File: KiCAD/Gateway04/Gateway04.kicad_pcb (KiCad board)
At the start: 2 copper layers, 53 x 53 mm, 8 parts, among them U1 LSHM, U2 LSHM, U3 LSHM, U4 LSHM, U5 LSHM, U6 LSHM, U7 LSHM, U8 LSHM

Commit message: finished Gateway04
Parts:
- U1, U2, U3, U4, U5, U6, U7, U8: footprint Gateway03:LSHM-120-02.5-L-DV-A-S-TR -> Gateway04:LSHM-120-02.5-L-DV-A-S-TR
- moved U1 0.50 mm to (85.2, 83.8)
- moved U3 0.50 mm to (102.5, 83.8)
- moved U6 0.50 mm to (85.2, 110.7)
- moved U8 0.50 mm to (102.5, 110.7)
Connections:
- U1 pad 40: Net-(U1-Pad40) -> GND
- U2 pad 10: Net-(U1-Pad10) -> Net-(U1-Pad8)
- U2 pad 12: Net-(U1-Pad12) -> Net-(U1-Pad10)
- U2 pad 14: Net-(U1-Pad14) -> Net-(U1-Pad12)
- U2 pad 16: Net-(U1-Pad16) -> Net-(U1-Pad14)
- U2 pad 18: Net-(U1-Pad18) -> Net-(U1-Pad16)
- U2 pad 2: Net-(U1-Pad2) -> GND
- U2 pad 20: Net-(U1-Pad20) -> Net-(U1-Pad18)
- U2 pad 22: Net-(U1-Pad22) -> Net-(U1-Pad20)
- U2 pad 24: Net-(U1-Pad24) -> Net-(U1-Pad22)
- U2 pad 26: Net-(U1-Pad26) -> Net-(U1-Pad24)
- U2 pad 28: Net-(U1-Pad28) -> Net-(U1-Pad26)
- U2 pad 30: Net-(U1-Pad30) -> Net-(U1-Pad28)
- U2 pad 32: Net-(U1-Pad32) -> Net-(U1-Pad30)
- U2 pad 34: Net-(U1-Pad34) -> Net-(U1-Pad32)
- U2 pad 36: Net-(U1-Pad36) -> Net-(U1-Pad34)
- U2 pad 38: Net-(U1-Pad38) -> Net-(U1-Pad36)
- U2 pad 4: Net-(U1-Pad4) -> Net-(U1-Pad2)
- U2 pad 40: Net-(U1-Pad40) -> Net-(U1-Pad38)
- U2 pad 6: Net-(U1-Pad6) -> Net-(U1-Pad4)
- U2 pad 8: Net-(U1-Pad8) -> Net-(U1-Pad6)
- U3 pad 40: Net-(U3-Pad40) -> GND
- U4 pad 10: Net-(U3-Pad10) -> Net-(U3-Pad8)
- U4 pad 12: Net-(U3-Pad12) -> Net-(U3-Pad10)
- U4 pad 14: Net-(U3-Pad14) -> Net-(U3-Pad12)
- U4 pad 16: Net-(U3-Pad16) -> Net-(U3-Pad14)
- U4 pad 18: Net-(U3-Pad18) -> Net-(U3-Pad16)
- U4 pad 2: Net-(U3-Pad2) -> GND
- U4 pad 20: Net-(U3-Pad20) -> Net-(U3-Pad18)
- U4 pad 22: Net-(U3-Pad22) -> Net-(U3-Pad20)
- U4 pad 24: Net-(U3-Pad24) -> Net-(U3-Pad22)
- U4 pad 26: Net-(U3-Pad26) -> Net-(U3-Pad24)
- U4 pad 28: Net-(U3-Pad28) -> Net-(U3-Pad26)
- U4 pad 30: Net-(U3-Pad30) -> Net-(U3-Pad28)
- U4 pad 32: Net-(U3-Pad32) -> Net-(U3-Pad30)
- U4 pad 34: Net-(U3-Pad34) -> Net-(U3-Pad32)
- U4 pad 36: Net-(U3-Pad36) -> Net-(U3-Pad34)
- U4 pad 38: Net-(U3-Pad38) -> Net-(U3-Pad36)
- U4 pad 4: Net-(U3-Pad4) -> Net-(U3-Pad2)
- U4 pad 40: Net-(U3-Pad40) -> Net-(U3-Pad38)
- U4 pad 6: Net-(U3-Pad6) -> Net-(U3-Pad4)
- U4 pad 8: Net-(U3-Pad8) -> Net-(U3-Pad6)
- U5 pad 40: Net-(U5-Pad40) -> GND
- U6 pad 10: Net-(U5-Pad10) -> Net-(U5-Pad8)
- U6 pad 12: Net-(U5-Pad12) -> Net-(U5-Pad10)
- U6 pad 14: Net-(U5-Pad14) -> Net-(U5-Pad12)
- U6 pad 16: Net-(U5-Pad16) -> Net-(U5-Pad14)
- U6 pad 18: Net-(U5-Pad18) -> Net-(U5-Pad16)
- U6 pad 2: Net-(U5-Pad2) -> GND
- U6 pad 20: Net-(U5-Pad20) -> Net-(U5-Pad18)
- U6 pad 22: Net-(U5-Pad22) -> Net-(U5-Pad20)
- U6 pad 24: Net-(U5-Pad24) -> Net-(U5-Pad22)
- U6 pad 26: Net-(U5-Pad26) -> Net-(U5-Pad24)
- U6 pad 28: Net-(U5-Pad28) -> Net-(U5-Pad26)
- U6 pad 30: Net-(U5-Pad30) -> Net-(U5-Pad28)
- U6 pad 32: Net-(U5-Pad32) -> Net-(U5-Pad30)
- U6 pad 34: Net-(U5-Pad34) -> Net-(U5-Pad32)
- U6 pad 36: Net-(U5-Pad36) -> Net-(U5-Pad34)
- U6 pad 38: Net-(U5-Pad38) -> Net-(U5-Pad36)
- U6 pad 4: Net-(U5-Pad4) -> Net-(U5-Pad2)
- U6 pad 40: Net-(U5-Pad40) -> Net-(U5-Pad38)
- U6 pad 6: Net-(U5-Pad6) -> Net-(U5-Pad4)
- U6 pad 8: Net-(U5-Pad8) -> Net-(U5-Pad6)
- U7 pad 40: Net-(U7-Pad40) -> GND
- U8 pad 10: Net-(U7-Pad10) -> Net-(U7-Pad8)
- U8 pad 12: Net-(U7-Pad12) -> Net-(U7-Pad10)
- U8 pad 14: Net-(U7-Pad14) -> Net-(U7-Pad12)
- U8 pad 16: Net-(U7-Pad16) -> Net-(U7-Pad14)
- U8 pad 18: Net-(U7-Pad18) -> Net-(U7-Pad16)
- U8 pad 2: Net-(U7-Pad2) -> GND
- U8 pad 20: Net-(U7-Pad20) -> Net-(U7-Pad18)
- U8 pad 22: Net-(U7-Pad22) -> Net-(U7-Pad20)
- U8 pad 24: Net-(U7-Pad24) -> Net-(U7-Pad22)
- U8 pad 26: Net-(U7-Pad26) -> Net-(U7-Pad24)
- U8 pad 28: Net-(U7-Pad28) -> Net-(U7-Pad26)
- U8 pad 30: Net-(U7-Pad30) -> Net-(U7-Pad28)
- U8 pad 32: Net-(U7-Pad32) -> Net-(U7-Pad30)
- U8 pad 34: Net-(U7-Pad34) -> Net-(U7-Pad32)
- U8 pad 36: Net-(U7-Pad36) -> Net-(U7-Pad34)
- U8 pad 38: Net-(U7-Pad38) -> Net-(U7-Pad36)
- U8 pad 4: Net-(U7-Pad4) -> Net-(U7-Pad2)
- U8 pad 40: Net-(U7-Pad40) -> Net-(U7-Pad38)
- U8 pad 6: Net-(U7-Pad6) -> Net-(U7-Pad4)
- U8 pad 8: Net-(U7-Pad8) -> Net-(U7-Pad6)
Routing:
- net Net-(U5-Pad40): track 8.09 -> 0.00 mm, vias 1 -> 0
- net Net-(U3-Pad2): track 0.00 -> 7.28 mm, vias 0 -> 1
- net Net-(U3-Pad38): track 0.16 -> 7.34 mm
- net Net-(U7-Pad40): track 7.09 -> 0.00 mm, vias 1 -> 0
- net Net-(U1-Pad40): track 7.09 -> 0.00 mm, vias 1 -> 0
- net Net-(U3-Pad6): track 0.00 -> 6.76 mm
- net Net-(U3-Pad34): track 0.00 -> 6.75 mm
- net Net-(U3-Pad4): track 0.16 -> 6.90 mm
- net Net-(U3-Pad8): track 0.00 -> 6.63 mm
- net Net-(U3-Pad36): track 0.29 -> 6.90 mm
- net Net-(U3-Pad32): track 0.00 -> 6.61 mm
- net Net-(U3-Pad10): track 0.00 -> 6.49 mm
- net Net-(U3-Pad30): track 0.00 -> 6.47 mm
- net Net-(U3-Pad12): track 0.00 -> 6.35 mm
- net Net-(U3-Pad28): track 0.00 -> 6.34 mm
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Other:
- board text added: "Feb 2020"
- board text added: "Gateway04"
- board text removed: "Gateway03"
- board text removed: "Nov 2019"

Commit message: created gateway04
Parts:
- U1, U2, U3, U4, U5, U6, U7, U8: value LSHM -> LSHM-120-02.5-L-DV-A-S-TR; footprint Gateway04:LSHM-120-02.5-L-DV-A-S-TR -> Gateway03:LSHM-120-02.5-L-DV-A-S-TR
- moved U1 2.12 mm to (83.7, 85.3)
- moved U3 2.12 mm to (104.0, 85.3)
- moved U6 2.12 mm to (83.7, 109.2)
- moved U8 2.12 mm to (104.0, 109.2)
- moved U2 1.80 mm to (83.7, 94.8)
- moved U4 1.80 mm to (104.0, 94.8)
- moved U5 1.80 mm to (83.7, 99.7)
- moved U7 1.80 mm to (104.0, 99.7)
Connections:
- U1 pad 40: GND -> Net-(U1-Pad40)
- U2 pad 10: Net-(U1-Pad8) -> Net-(U1-Pad10)
- U2 pad 12: Net-(U1-Pad10) -> Net-(U1-Pad12)
- U2 pad 14: Net-(U1-Pad12) -> Net-(U1-Pad14)
- U2 pad 16: Net-(U1-Pad14) -> Net-(U1-Pad16)
- U2 pad 18: Net-(U1-Pad16) -> Net-(U1-Pad18)
- U2 pad 2: GND -> Net-(U1-Pad2)
- U2 pad 20: Net-(U1-Pad18) -> Net-(U1-Pad20)
- U2 pad 22: Net-(U1-Pad20) -> Net-(U1-Pad22)
- U2 pad 24: Net-(U1-Pad22) -> Net-(U1-Pad24)
- U2 pad 26: Net-(U1-Pad24) -> Net-(U1-Pad26)
- U2 pad 28: Net-(U1-Pad26) -> Net-(U1-Pad28)
- U2 pad 30: Net-(U1-Pad28) -> Net-(U1-Pad30)
- U2 pad 32: Net-(U1-Pad30) -> Net-(U1-Pad32)
- U2 pad 34: Net-(U1-Pad32) -> Net-(U1-Pad34)
- U2 pad 36: Net-(U1-Pad34) -> Net-(U1-Pad36)
- U2 pad 38: Net-(U1-Pad36) -> Net-(U1-Pad38)
- U2 pad 4: Net-(U1-Pad2) -> Net-(U1-Pad4)
- U2 pad 40: Net-(U1-Pad38) -> Net-(U1-Pad40)
- U2 pad 6: Net-(U1-Pad4) -> Net-(U1-Pad6)
- U2 pad 8: Net-(U1-Pad6) -> Net-(U1-Pad8)
- U3 pad 40: GND -> Net-(U3-Pad40)
- U4 pad 10: Net-(U3-Pad8) -> Net-(U3-Pad10)
- U4 pad 12: Net-(U3-Pad10) -> Net-(U3-Pad12)
- U4 pad 14: Net-(U3-Pad12) -> Net-(U3-Pad14)
- U4 pad 16: Net-(U3-Pad14) -> Net-(U3-Pad16)
- U4 pad 18: Net-(U3-Pad16) -> Net-(U3-Pad18)
- U4 pad 2: GND -> Net-(U3-Pad2)
- U4 pad 20: Net-(U3-Pad18) -> Net-(U3-Pad20)
- U4 pad 22: Net-(U3-Pad20) -> Net-(U3-Pad22)
- U4 pad 24: Net-(U3-Pad22) -> Net-(U3-Pad24)
- U4 pad 26: Net-(U3-Pad24) -> Net-(U3-Pad26)
- U4 pad 28: Net-(U3-Pad26) -> Net-(U3-Pad28)
- U4 pad 30: Net-(U3-Pad28) -> Net-(U3-Pad30)
- U4 pad 32: Net-(U3-Pad30) -> Net-(U3-Pad32)
- U4 pad 34: Net-(U3-Pad32) -> Net-(U3-Pad34)
- U4 pad 36: Net-(U3-Pad34) -> Net-(U3-Pad36)
- U4 pad 38: Net-(U3-Pad36) -> Net-(U3-Pad38)
- U4 pad 4: Net-(U3-Pad2) -> Net-(U3-Pad4)
- U4 pad 40: Net-(U3-Pad38) -> Net-(U3-Pad40)
- U4 pad 6: Net-(U3-Pad4) -> Net-(U3-Pad6)
- U4 pad 8: Net-(U3-Pad6) -> Net-(U3-Pad8)
- U5 pad 40: GND -> Net-(U5-Pad40)
- U6 pad 10: Net-(U5-Pad8) -> Net-(U5-Pad10)
- U6 pad 12: Net-(U5-Pad10) -> Net-(U5-Pad12)
- U6 pad 14: Net-(U5-Pad12) -> Net-(U5-Pad14)
- U6 pad 16: Net-(U5-Pad14) -> Net-(U5-Pad16)
- U6 pad 18: Net-(U5-Pad16) -> Net-(U5-Pad18)
- U6 pad 2: GND -> Net-(U5-Pad2)
- U6 pad 20: Net-(U5-Pad18) -> Net-(U5-Pad20)
- U6 pad 22: Net-(U5-Pad20) -> Net-(U5-Pad22)
- U6 pad 24: Net-(U5-Pad22) -> Net-(U5-Pad24)
- U6 pad 26: Net-(U5-Pad24) -> Net-(U5-Pad26)
- U6 pad 28: Net-(U5-Pad26) -> Net-(U5-Pad28)
- U6 pad 30: Net-(U5-Pad28) -> Net-(U5-Pad30)
- U6 pad 32: Net-(U5-Pad30) -> Net-(U5-Pad32)
- U6 pad 34: Net-(U5-Pad32) -> Net-(U5-Pad34)
- U6 pad 36: Net-(U5-Pad34) -> Net-(U5-Pad36)
- U6 pad 38: Net-(U5-Pad36) -> Net-(U5-Pad38)
- U6 pad 4: Net-(U5-Pad2) -> Net-(U5-Pad4)
- U6 pad 40: Net-(U5-Pad38) -> Net-(U5-Pad40)
- U6 pad 6: Net-(U5-Pad4) -> Net-(U5-Pad6)
- U6 pad 8: Net-(U5-Pad6) -> Net-(U5-Pad8)
- U7 pad 40: GND -> Net-(U7-Pad40)
- U8 pad 10: Net-(U7-Pad8) -> Net-(U7-Pad10)
- U8 pad 12: Net-(U7-Pad10) -> Net-(U7-Pad12)
- U8 pad 14: Net-(U7-Pad12) -> Net-(U7-Pad14)
- U8 pad 16: Net-(U7-Pad14) -> Net-(U7-Pad16)
- U8 pad 18: Net-(U7-Pad16) -> Net-(U7-Pad18)
- U8 pad 2: GND -> Net-(U7-Pad2)
- U8 pad 20: Net-(U7-Pad18) -> Net-(U7-Pad20)
- U8 pad 22: Net-(U7-Pad20) -> Net-(U7-Pad22)
- U8 pad 24: Net-(U7-Pad22) -> Net-(U7-Pad24)
- U8 pad 26: Net-(U7-Pad24) -> Net-(U7-Pad26)
- U8 pad 28: Net-(U7-Pad26) -> Net-(U7-Pad28)
- U8 pad 30: Net-(U7-Pad28) -> Net-(U7-Pad30)
- U8 pad 32: Net-(U7-Pad30) -> Net-(U7-Pad32)
- U8 pad 34: Net-(U7-Pad32) -> Net-(U7-Pad34)
- U8 pad 36: Net-(U7-Pad34) -> Net-(U7-Pad36)
- U8 pad 38: Net-(U7-Pad36) -> Net-(U7-Pad38)
- U8 pad 4: Net-(U7-Pad2) -> Net-(U7-Pad4)
- U8 pad 40: Net-(U7-Pad38) -> Net-(U7-Pad40)
- U8 pad 6: Net-(U7-Pad4) -> Net-(U7-Pad6)
- U8 pad 8: Net-(U7-Pad6) -> Net-(U7-Pad8)
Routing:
- net Net-(U5-Pad40): track 0.00 -> 8.09 mm, vias 0 -> 1
- net Net-(U3-Pad40): track 0.00 -> 7.09 mm, vias 0 -> 1
- net Net-(U7-Pad40): track 0.00 -> 7.09 mm, vias 0 -> 1
- net Net-(U1-Pad40): track 0.00 -> 7.09 mm, vias 0 -> 1
- net Net-(U3-Pad2): track 7.28 -> 4.95 mm, vias 1 -> 0
- net Net-(U3-Pad4): track 6.90 -> 8.59 mm, vias 1 -> 2
- net GND: track 1.00 -> 0.00 mm
- net Net-(U7-Pad38): track 7.34 -> 6.48 mm
- net Net-(U3-Pad38): track 7.34 -> 6.48 mm
- net Net-(U5-Pad38): track 8.47 -> 7.61 mm
- net Net-(U1-Pad38): track 7.34 -> 6.48 mm
- net Net-(U7-Pad22): track 6.01 -> 5.37 mm
- net Net-(U5-Pad22): track 6.01 -> 5.37 mm
- net Net-(U3-Pad22): track 6.01 -> 5.37 mm
- net Net-(U1-Pad22): track 6.01 -> 5.37 mm
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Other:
- board text added: "Gateway03"
- board text added: "Nov 2019"
- board text removed: "Feb 2020"
- board text removed: "Gateway04"

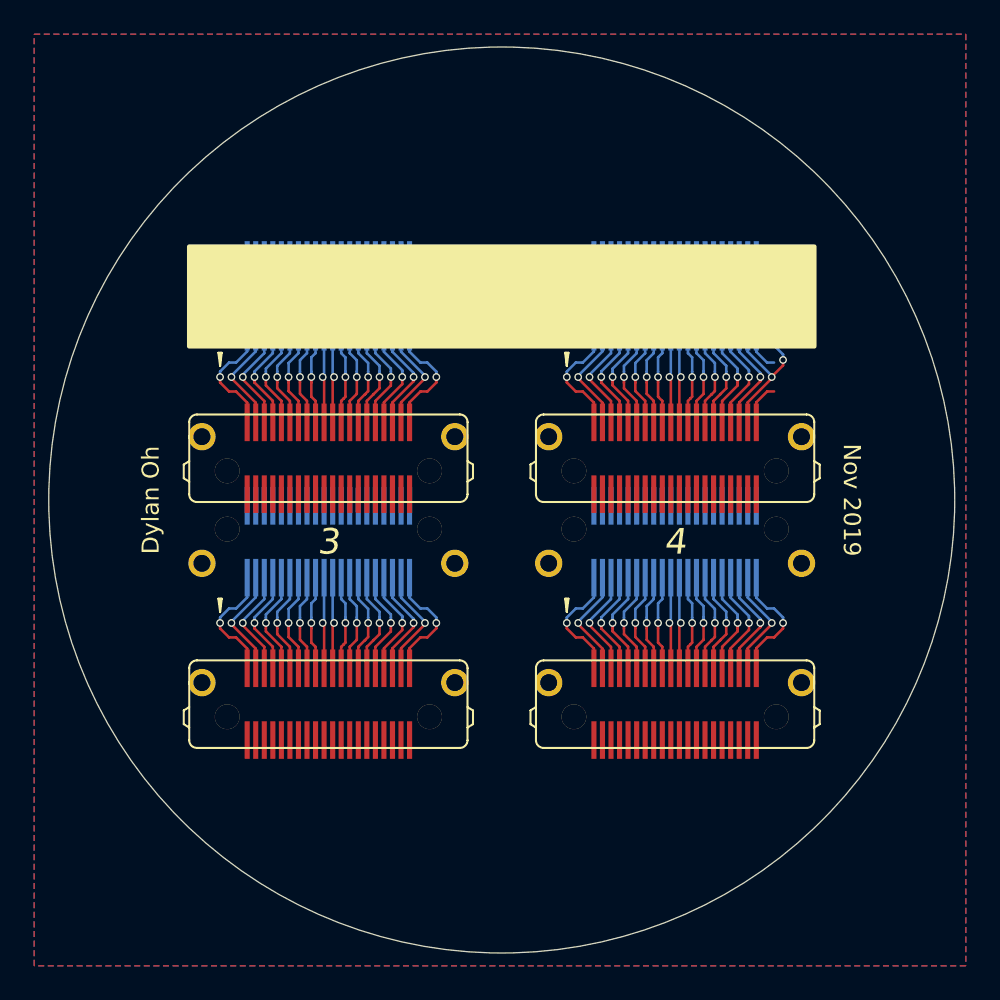
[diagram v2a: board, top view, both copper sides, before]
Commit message: finished Gateway04, added silkscreen
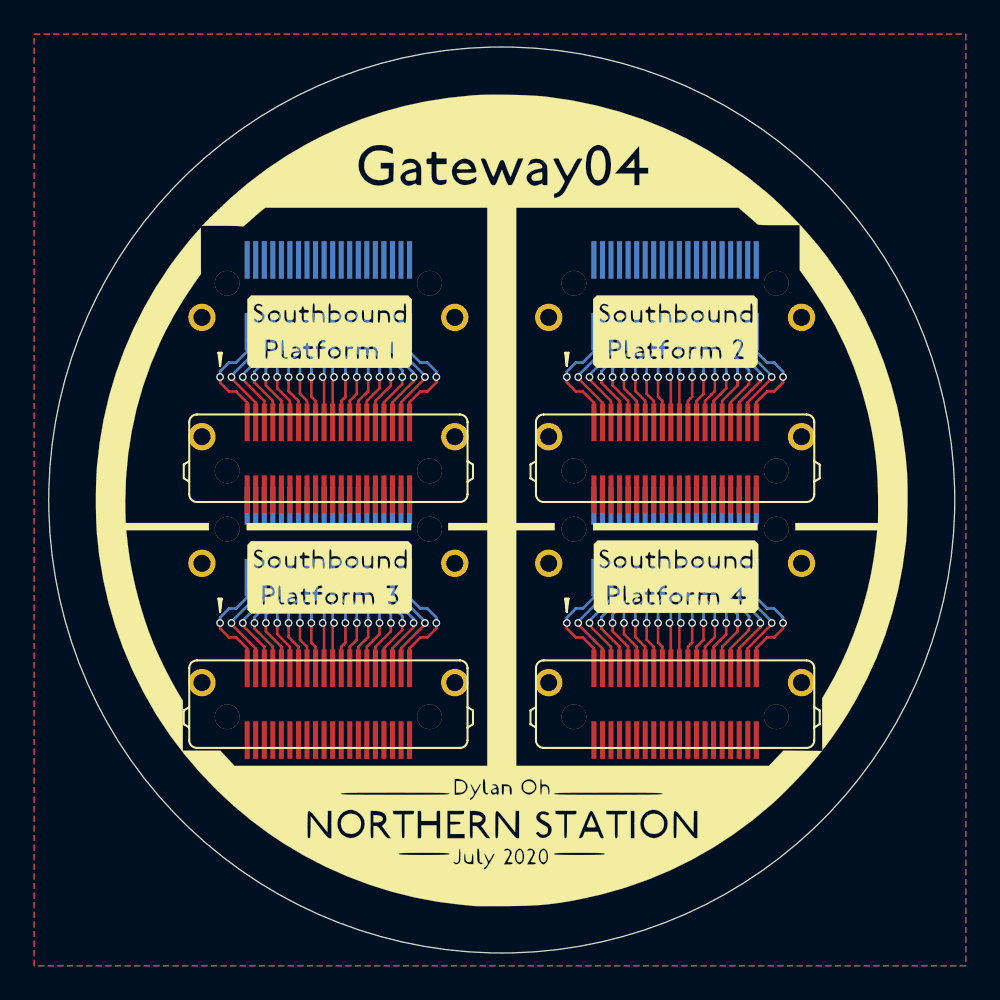
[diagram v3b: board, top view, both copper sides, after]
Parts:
- added G***: LOGO, Gateway04:southern_station, B.Cu at (93.9, 97.3)
- added G***: LOGO, Gateway04:northern_station, F.Cu at (93.9, 97.3)
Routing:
- net Net-(U3-Pad4): track 8.59 -> 6.46 mm, vias 2 -> 1
- net Net-(U3-Pad2): track 4.95 -> 7.07 mm, vias 0 -> 1
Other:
- board text removed: "1"
- board text removed: "2"
- board text removed: "3"
- board text removed: "4"
- board text removed: "Dylan Oh"
- board text removed: "Entrance"
- board text removed: "Exit"
- board text removed: "Gateway03"
- board text removed: "Nov 2019"

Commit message: finished Gateway04
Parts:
- removed the G*** at (93.9, 97.3) (x2)
- added G***: LOGO, Gateway04:south, B.Cu at (93.9, 97.3)
- added G***: LOGO, Gateway04:north, F.Cu at (93.9, 97.3)
- moved U1 1.00 mm to (83.7, 86.3)
- moved U2 1.00 mm to (83.7, 95.8)
- moved U3 1.00 mm to (104.0, 86.3)
- moved U4 1.00 mm to (104.0, 95.8)
- moved U5 1.00 mm to (83.7, 100.7)
- moved U6 1.00 mm to (83.7, 110.2)
- moved U7 1.00 mm to (104.0, 100.7)
- moved U8 1.00 mm to (104.0, 110.2)
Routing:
- net GND: track 0.00 -> 436.2 mm

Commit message: update
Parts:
- U1, U2, U3, U4, U5, U6, U7, U8: value LSHM-120-02.5-L-DV-A-S-TR -> LSHM; footprint Gateway03:LSHM-120-02.5-L-DV-A-S-TR -> Gateway04:LSHM-120-02.5-L-DV-A-S-TR
